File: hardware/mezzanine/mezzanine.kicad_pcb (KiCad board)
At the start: 4 copper layers, 85 x 56 mm, 34 parts, among them J1 USB_A, J2 USB_C, J3 HDMI_D, J4 HDMI_D, U1 AP22653W6, U2 TPD4EUSB30, U3 TPD4EUSB30, U4 TPD4EUSB30, U5 MagJack-A70-112-331N126, U6 RT9742SNGV, U7 74LVC1G07SE-7

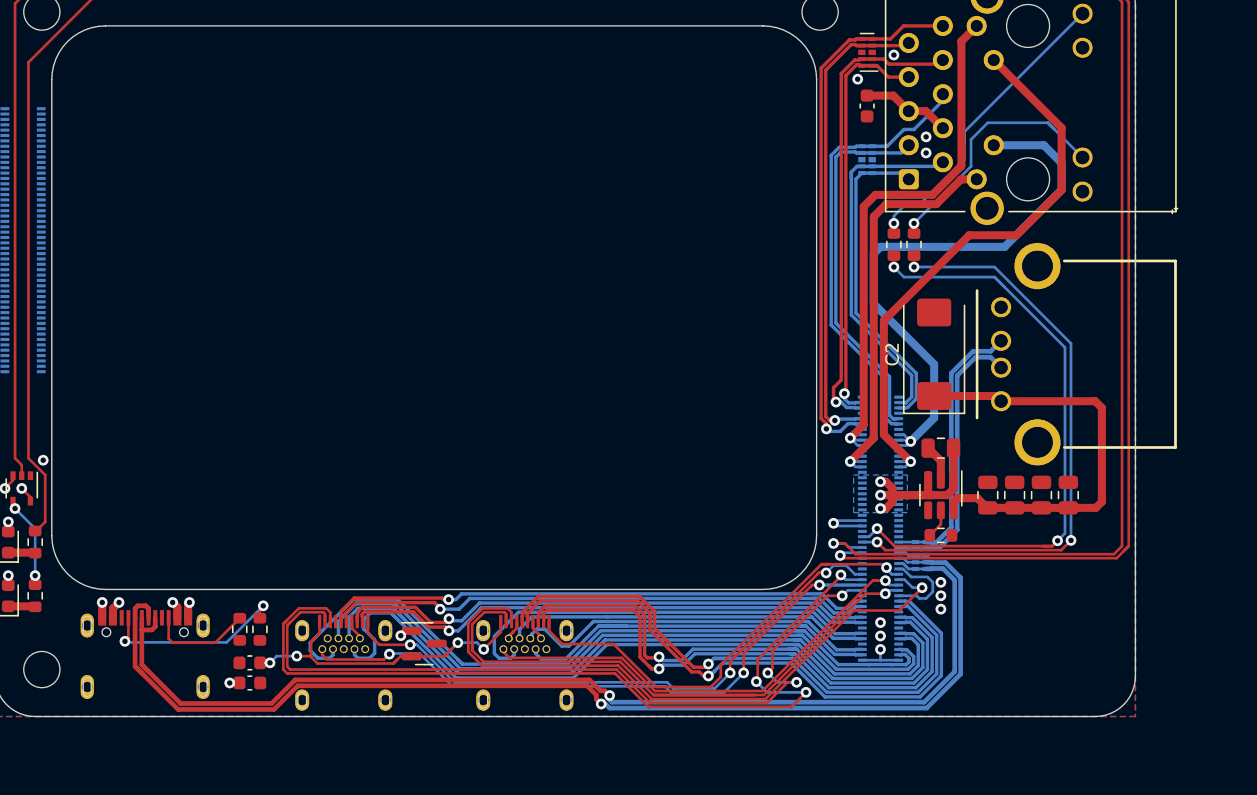
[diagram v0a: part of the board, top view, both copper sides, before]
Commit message: tweak mezzanine
almost ready to order
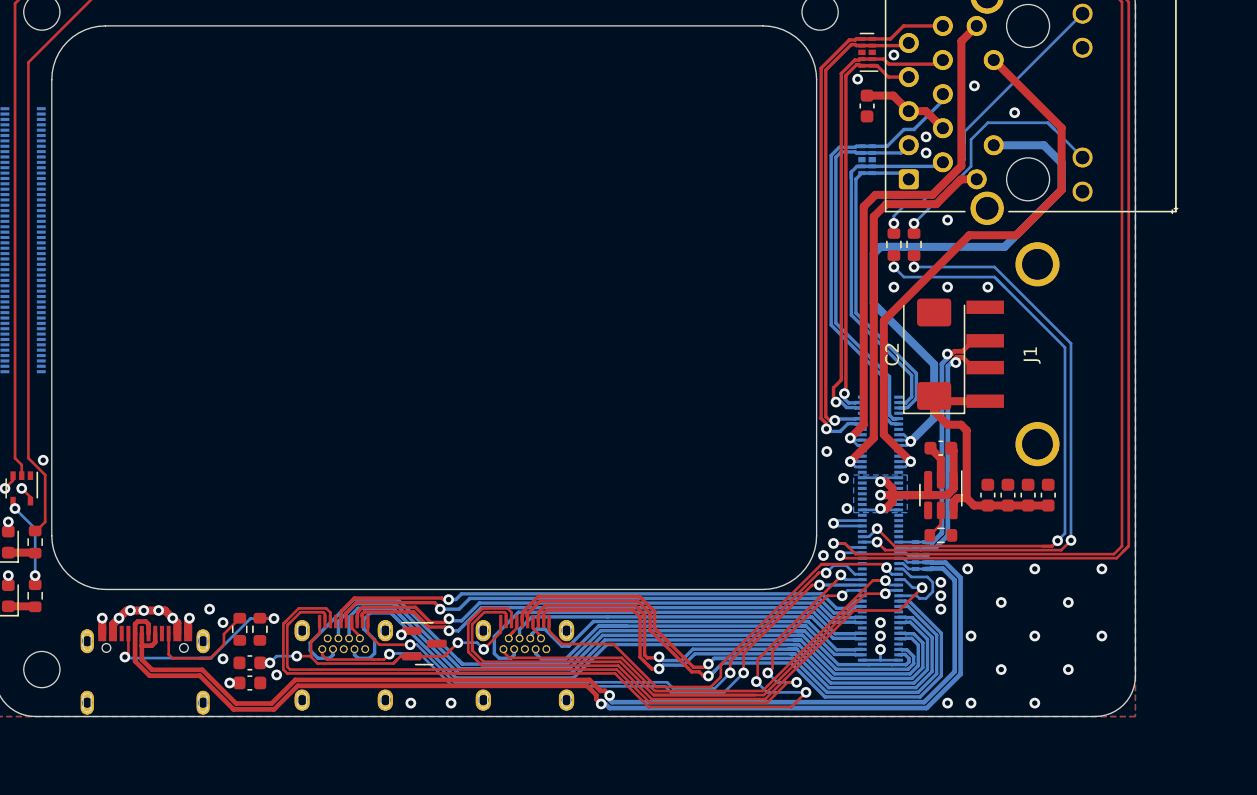
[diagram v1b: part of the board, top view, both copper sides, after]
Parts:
- C1, C3, C4, C5, C6: footprint Capacitor_SMD:C_0805_2012Metric -> Capacitor_SMD:C_0603_1608Metric
- J1: footprint cm4crypto:OnShore_USB-A1HSB6 -> cm4crypto:AU-Y1006
- R1: value 15K -> 15K 1%
- moved C6 1.50 mm to (98.5, 59.5)
- moved J2 1.17 mm to (31.2, 77.2)
- moved C4 1.00 mm to (97.0, 59.5)
- moved C5 0.50 mm to (95.5, 59.5)
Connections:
- net /usb/+5v renamed +5v
- J3 pad 2: unconnected-(J3-Pad2) -> (no net)
- J4 pad 2: unconnected-(J4-Pad2) -> (no net)
- Module1 pad 49: /AnalogIP1 -> (no net)
- Module1 pad 51: /AnalogIP0 -> (no net)
- Module2 pad 1: unconnected-(Module2-Pad1) -> (no net)
- Module2 pad 10: unconnected-(Module2-Pad10) -> (no net)
- Module2 pad 100: unconnected-(Module2-Pad100) -> (no net)
- Module2 pad 11: unconnected-(Module2-Pad11) -> (no net)
- Module2 pad 12: unconnected-(Module2-Pad12) -> (no net)
- Module2 pad 13: unconnected-(Module2-Pad13) -> (no net)
- Module2 pad 14: unconnected-(Module2-Pad14) -> (no net)
- Module2 pad 15: unconnected-(Module2-Pad15) -> (no net)
- Module2 pad 16: unconnected-(Module2-Pad16) -> (no net)
- Module2 pad 17: unconnected-(Module2-Pad17) -> (no net)
- Module2 pad 18: unconnected-(Module2-Pad18) -> (no net)
- Module2 pad 19: unconnected-(Module2-Pad19) -> (no net)
- Module2 pad 2: unconnected-(Module2-Pad2) -> (no net)
- Module2 pad 20: unconnected-(Module2-Pad20) -> (no net)
- Module2 pad 21: unconnected-(Module2-Pad21) -> (no net)
- Module2 pad 22: unconnected-(Module2-Pad22) -> (no net)
- Module2 pad 23: unconnected-(Module2-Pad23) -> (no net)
- Module2 pad 24: unconnected-(Module2-Pad24) -> (no net)
- Module2 pad 25: unconnected-(Module2-Pad25) -> (no net)
- Module2 pad 26: unconnected-(Module2-Pad26) -> (no net)
- Module2 pad 27: unconnected-(Module2-Pad27) -> (no net)
- Module2 pad 28: unconnected-(Module2-Pad28) -> (no net)
- Module2 pad 29: unconnected-(Module2-Pad29) -> (no net)
- Module2 pad 3: unconnected-(Module2-Pad3) -> (no net)
- Module2 pad 30: unconnected-(Module2-Pad30) -> (no net)
- Module2 pad 31: unconnected-(Module2-Pad31) -> (no net)
- Module2 pad 32: unconnected-(Module2-Pad32) -> (no net)
- Module2 pad 33: unconnected-(Module2-Pad33) -> (no net)
- Module2 pad 34: unconnected-(Module2-Pad34) -> (no net)
- Module2 pad 35: unconnected-(Module2-Pad35) -> (no net)
- Module2 pad 36: unconnected-(Module2-Pad36) -> (no net)
- Module2 pad 37: unconnected-(Module2-Pad37) -> (no net)
- Module2 pad 38: unconnected-(Module2-Pad38) -> (no net)
- Module2 pad 39: unconnected-(Module2-Pad39) -> (no net)
- Module2 pad 4: unconnected-(Module2-Pad4) -> (no net)
- Module2 pad 40: unconnected-(Module2-Pad40) -> (no net)
- Module2 pad 41: unconnected-(Module2-Pad41) -> (no net)
- Module2 pad 42: unconnected-(Module2-Pad42) -> (no net)
- Module2 pad 43: unconnected-(Module2-Pad43) -> (no net)
- Module2 pad 44: unconnected-(Module2-Pad44) -> (no net)
- Module2 pad 45: unconnected-(Module2-Pad45) -> (no net)
- Module2 pad 46: unconnected-(Module2-Pad46) -> (no net)
- Module2 pad 47: unconnected-(Module2-Pad47) -> (no net)
- Module2 pad 48: unconnected-(Module2-Pad48) -> (no net)
- Module2 pad 49: unconnected-(Module2-Pad49) -> (no net)
- Module2 pad 5: unconnected-(Module2-Pad5) -> (no net)
- Module2 pad 50: unconnected-(Module2-Pad50) -> (no net)
- Module2 pad 51: unconnected-(Module2-Pad51) -> (no net)
- Module2 pad 52: unconnected-(Module2-Pad52) -> (no net)
- Module2 pad 53: unconnected-(Module2-Pad53) -> (no net)
- Module2 pad 54: unconnected-(Module2-Pad54) -> (no net)
- Module2 pad 55: unconnected-(Module2-Pad55) -> (no net)
- Module2 pad 56: unconnected-(Module2-Pad56) -> (no net)
- Module2 pad 57: unconnected-(Module2-Pad57) -> (no net)
- Module2 pad 58: unconnected-(Module2-Pad58) -> (no net)
- Module2 pad 59: unconnected-(Module2-Pad59) -> (no net)
- Module2 pad 6: unconnected-(Module2-Pad6) -> (no net)
- Module2 pad 60: unconnected-(Module2-Pad60) -> (no net)
- Module2 pad 61: unconnected-(Module2-Pad61) -> (no net)
- Module2 pad 62: unconnected-(Module2-Pad62) -> (no net)
- Module2 pad 63: unconnected-(Module2-Pad63) -> (no net)
- Module2 pad 64: unconnected-(Module2-Pad64) -> (no net)
- Module2 pad 65: unconnected-(Module2-Pad65) -> (no net)
- Module2 pad 66: unconnected-(Module2-Pad66) -> (no net)
- Module2 pad 67: unconnected-(Module2-Pad67) -> (no net)
- Module2 pad 68: unconnected-(Module2-Pad68) -> (no net)
- Module2 pad 69: unconnected-(Module2-Pad69) -> (no net)
- Module2 pad 7: unconnected-(Module2-Pad7) -> (no net)
- Module2 pad 70: unconnected-(Module2-Pad70) -> (no net)
- Module2 pad 71: unconnected-(Module2-Pad71) -> (no net)
- Module2 pad 72: unconnected-(Module2-Pad72) -> (no net)
- Module2 pad 73: unconnected-(Module2-Pad73) -> (no net)
- Module2 pad 74: unconnected-(Module2-Pad74) -> (no net)
- Module2 pad 75: unconnected-(Module2-Pad75) -> (no net)
- Module2 pad 76: unconnected-(Module2-Pad76) -> (no net)
- Module2 pad 77: unconnected-(Module2-Pad77) -> (no net)
- Module2 pad 78: unconnected-(Module2-Pad78) -> (no net)
- Module2 pad 79: unconnected-(Module2-Pad79) -> (no net)
- Module2 pad 8: unconnected-(Module2-Pad8) -> (no net)
- Module2 pad 80: unconnected-(Module2-Pad80) -> (no net)
- Module2 pad 81: unconnected-(Module2-Pad81) -> (no net)
- Module2 pad 82: unconnected-(Module2-Pad82) -> (no net)
- Module2 pad 83: unconnected-(Module2-Pad83) -> (no net)
- Module2 pad 84: unconnected-(Module2-Pad84) -> (no net)
- Module2 pad 85: unconnected-(Module2-Pad85) -> (no net)
- Module2 pad 86: unconnected-(Module2-Pad86) -> (no net)
- Module2 pad 87: unconnected-(Module2-Pad87) -> (no net)
- Module2 pad 88: unconnected-(Module2-Pad88) -> (no net)
- Module2 pad 89: unconnected-(Module2-Pad89) -> (no net)
- Module2 pad 9: unconnected-(Module2-Pad9) -> (no net)
- Module2 pad 90: unconnected-(Module2-Pad90) -> (no net)
- Module2 pad 91: unconnected-(Module2-Pad91) -> (no net)
- Module2 pad 92: unconnected-(Module2-Pad92) -> (no net)
- Module2 pad 93: unconnected-(Module2-Pad93) -> (no net)
- Module2 pad 94: unconnected-(Module2-Pad94) -> (no net)
- Module2 pad 95: unconnected-(Module2-Pad95) -> (no net)
- Module2 pad 96: unconnected-(Module2-Pad96) -> (no net)
- Module2 pad 97: unconnected-(Module2-Pad97) -> (no net)
- Module2 pad 98: unconnected-(Module2-Pad98) -> (no net)
- Module2 pad 99: unconnected-(Module2-Pad99) -> (no net)
- U1 pad 4: /usb/nUSB_CURR_FAULT -> (no net)
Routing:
- net /usb/USB2_HOST_VBUS: track 32.2 -> 21.2 mm
- net +5v: track 50.0 -> 58.2 mm, vias 7 -> 10
- net /USB2_DEV_N: track 84.8 -> 82.7 mm
- net /USB2_DEV_P: track 82.1 -> 80.0 mm
- net Net-(R2-Pad1): track 14.4 -> 16.1 mm
- net Net-(R3-Pad1): track 7.74 -> 8.68 mm
- net /USB2_HOST_P: track 20.6 -> 20.3 mm, vias 0 -> 1
- net /USB2_HOST_N: track 20.7 -> 20.3 mm, vias 0 -> 1
- net GND: vias 13 -> 42

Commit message: update mezzanine
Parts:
- C2: footprint Capacitor_Tantalum_SMD:CP_EIA-7343-31_Kemet-D -> Capacitor_Tantalum_SMD:CP_EIA-2012-12_Kemet-R
- C7, C8, C9: value 100n -> 0.1 uF
- R1: value 15K 1% -> 14k
- moved C2 0.75 mm to (89.2, 49.0)
- moved C1 0.50 mm to (90.5, 56.5)
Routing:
- net /usb/USB2_HOST_VBUS: track 21.2 -> 25.0 mm
- net GND: track 23.4 -> 22.9 mm

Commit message: update mezzanine
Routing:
- net GND: vias 42 -> 49
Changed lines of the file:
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@@
       (outputformat 1)
       (mirror false)
-      (drillshape 1)
+      (drillshape 0)
       (scaleselection 1)
-      (outputdirectory "")
+      (outputdirectory "cam/")
     )
   )
@@
     (property "Sheetfile" "./sheets/usb.kicad_sch")
     (property "Sheetname" "usb")
-    (fp_text reference "J1" (at 0 -0.5 90 unlocked) (layer "F.SilkS")
+    (fp_text reference "J1" (at 0 -0.5 90 unlocked) (layer "F.SilkS") hide
       (effects (font (size 1 1) (thickness 0.15)))
     )
@@
     (fp_line (start -1 -0.3125) (end -1 0.625) (layer "F.Fab") (width 0.1))
     (fp_line (start -1 0.625) (end 1 0.625) (layer "F.Fab") (width 0.1))
-    (pad "1" smd roundrect locked (at -0.8875 0 90) (size 1.125 1.05) (layers "F.Cu" "F.Paste" "F.Mask") (roundrect_rratio 0.238095)
+    (pad "1" smd roundrect locked (at -0.8875 0 90) (size 1.125 1.05) (layers "F.Cu" "F.Paste" "F.Mask") (roundrect_rratio 0.2380952381)
       (net 2 "/usb/USB2_HOST_VBUS"))
-    (pad "2" smd roundrect locked (at 0.8875 0 90) (size 1.125 1.05) (layers "F.Cu" "F.Paste" "F.Mask") (roundrect_rratio 0.238095)
+    (pad "2" smd roundrect locked (at 0.8875 0 90) (size 1.125 1.05) (layers "F.Cu" "F.Paste" "F.Mask") (roundrect_rratio 0.2380952381)
       (net 1 "GND"))
     (model "${KICAD6_3DMODEL_DIR}/Capacitor_Tantalum_SMD.3dshapes/CP_EIA-2012-12_Kemet-R.wrl"
@@
   (via (at 100 72.5) (size 0.8) (drill 0.4) (layers "F.Cu" "B.Cu") (free) (net 1))
   (via (at 86 70) (size 0.8) (drill 0.4) (layers "F.Cu" "B.Cu") (free) (net 1))
+  (via (at 89.5 45) (size 0.8) (drill 0.4) (layers "F.Cu" "B.Cu") (free) (net 1))
   (via (at 51 75) (size 0.8) (drill 0.4) (layers "F.Cu" "B.Cu") (free) (net 1))
   (via (at 91 44) (size 0.8) (drill 0.4) (layers "F.Cu" "B.Cu") (free) (net 1))
@@
   (via (at 84.3 28.5) (size 0.8) (drill 0.4) (layers "F.Cu" "B.Cu") (free) (net 1))
   (via (at 41 72.9) (size 0.8) (drill 0.4) (layers "F.Cu" "B.Cu") (free) (net 1))
+  (via (at 90 39.5) (size 0.8) (drill 0.4) (layers "F.Cu" "B.Cu") (free) (net 1))
   (via (at 20.75 59) (size 0.8) (drill 0.4) (layers "F.Cu" "B.Cu") (net 1))
+  (via (at 88.5 46) (size 0.8) (drill 0.4) (layers "F.Cu" "B.Cu") (free) (net 1))
   (via (at 97.5 65) (size 0.8) (drill 0.4) (layers "F.Cu" "B.Cu") (free) (net 1))
+  (via (at 91.5 38) (size 0.8) (drill 0.4) (layers "F.Cu" "B.Cu") (free) (net 1))
   (via (at 92.75 70) (size 0.8) (drill 0.4) (layers "F.Cu" "B.Cu") (free) (net 1))
   (via (at 93 29) (size 0.8) (drill 0.4) (layers "F.Cu" "B.Cu") (free) (net 1))
@@
   (via (at 37 71.7) (size 0.8) (drill 0.4) (layers "F.Cu" "B.Cu") (free) (net 1))
   (via (at 102.5 65) (size 0.8) (drill 0.4) (layers "F.Cu" "B.Cu") (free) (net 1))
+  (via (at 94.5 35) (size 0.8) (drill 0.4) (layers "F.Cu" "B.Cu") (free) (net 1))
   (via (at 81.75 64) (size 0.8) (drill 0.4) (layers "F.Cu" "B.Cu") (free) (net 1))
   (via (at 92.5 65) (size 0.8) (drill 0.4) (layers "F.Cu" "B.Cu") (free) (net 1))
@@
   (via (at 54 75) (size 0.8) (drill 0.4) (layers "F.Cu" "B.Cu") (free) (net 1))
   (via (at 89.4 34) (size 0.8) (drill 0.4) (layers "F.Cu" "B.Cu") (free) (net 1))
+  (via (at 91 40) (size 0.8) (drill 0.4) (layers "F.Cu" "B.Cu") (free) (net 1))
   (via (at 90.5 66) (size 0.8) (drill 0.4) (layers "F.Cu" "B.Cu") (free) (net 1))
+  (via (at 90.5 46) (size 0.8) (drill 0.4) (layers "F.Cu" "B.Cu") (free) (net 1))
   (via (at 89.4 32.8) (size 0.8) (drill 0.4) (layers "F.Cu" "B.Cu") (free) (net 1))
   (via (at 95 72.5) (size 0.8) (drill 0.4) (layers "F.Cu" "B.Cu") (free) (net 1))

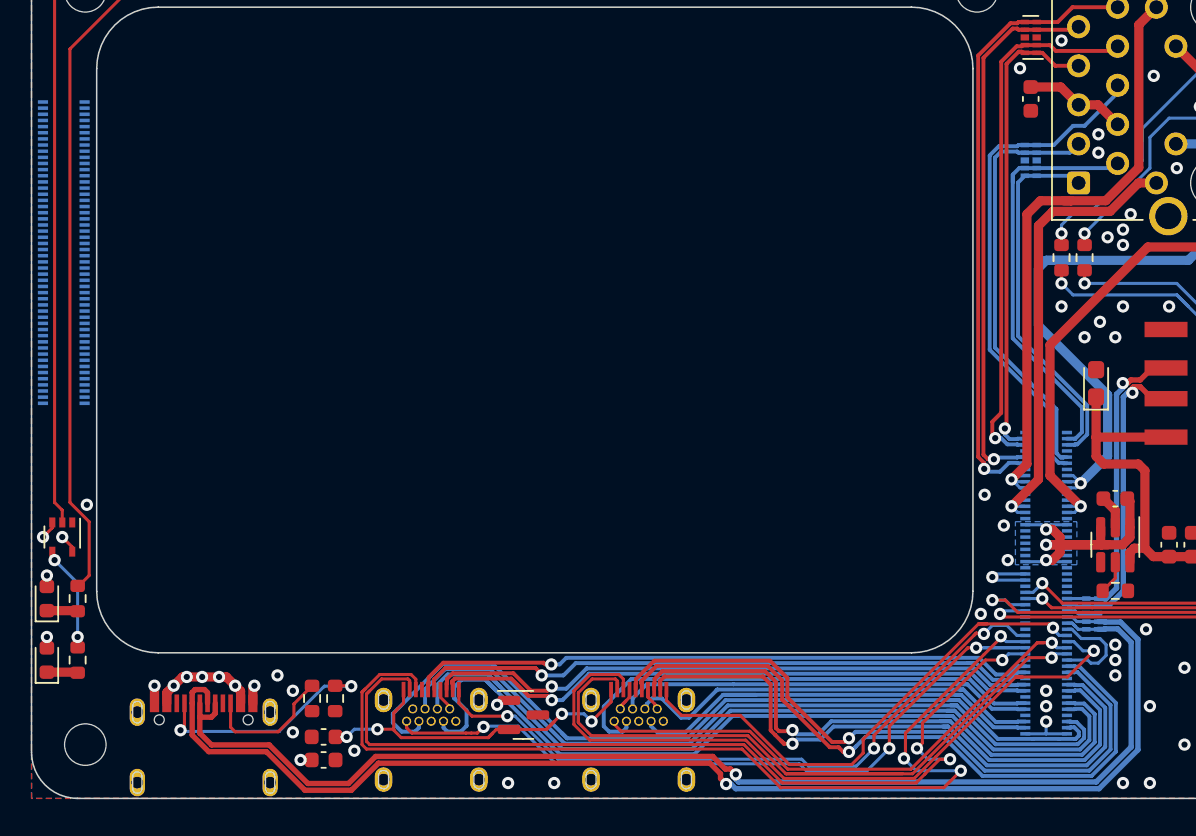
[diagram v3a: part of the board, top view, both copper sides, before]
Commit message: modify footprints
add paste on hdmi and usbc
add silkscreen outline on murata dcdc supply
change PS cap footprint to polarized footprint
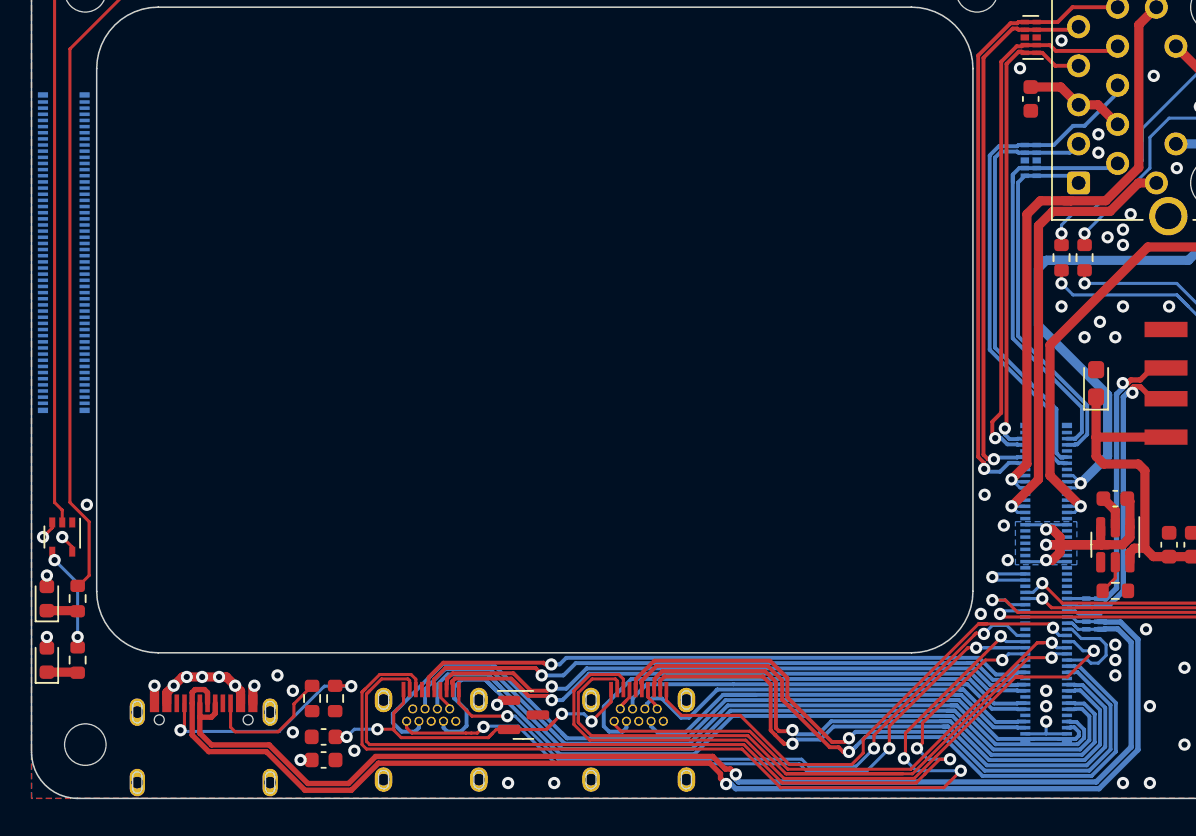
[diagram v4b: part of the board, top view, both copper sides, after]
